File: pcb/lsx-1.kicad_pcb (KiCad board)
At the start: 2 copper layers, 25.4 x 27.9 mm, 7 parts, among them J1 RJ45, J2 USART-USB, J3 ISP

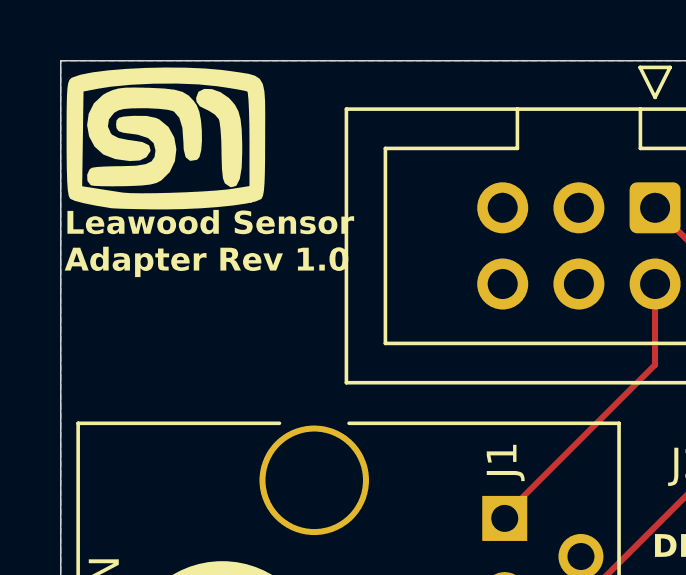
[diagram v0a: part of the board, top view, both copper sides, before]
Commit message: Corrects the GND on the ISP
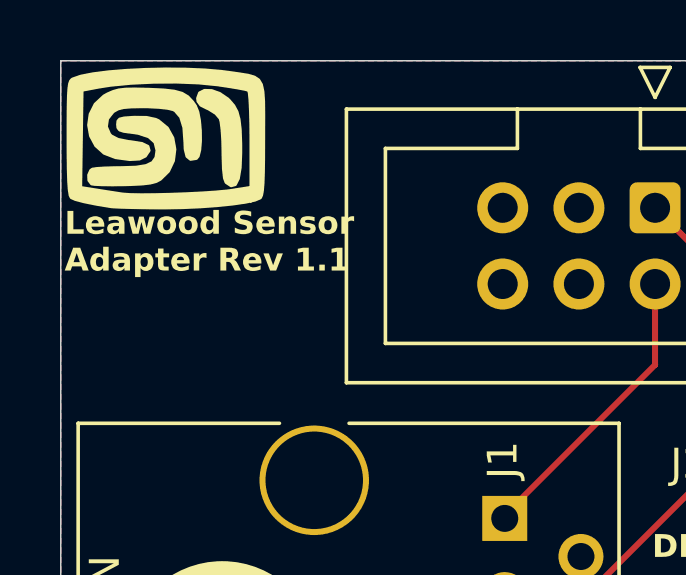
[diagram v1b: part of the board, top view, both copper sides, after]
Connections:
- J3 pad 6: unconnected-(J3-Pin_6-Pad6) -> GND
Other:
- board text added: "Leawood Sensor Adapter Rev 1.1"
- board text removed: "Leawood Sensor Adapter Rev 1.0"
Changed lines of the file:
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@@
 	(title_block
 		(title "Leawood Sensor Adapter LSX-1")
-		(date "2024-03-27")
-		(rev "1.0")
+		(date "2024-05-12")
+		(rev "1.1")
 	)
 	(layers
@@
 			(outputformat 1)
 			(mirror no)
-			(drillshape 1)
+			(drillshape 0)
 			(scaleselection 1)
-			(outputdirectory "")
+			(outputdirectory "lsx-Gerber/")
 		)
 	)
@@
 	(net 8 "unconnected-(J2-Pin_5-Pad5)")
 	(net 9 "unconnected-(J3-Pin_3-Pad3)")
-	(net 10 "unconnected-(J3-Pin_6-Pad6)")
-	(net 11 "unconnected-(J3-Pin_4-Pad4)")
-	(net 12 "unconnected-(J3-Pin_5-Pad5)")
+	(net 10 "unconnected-(J3-Pin_4-Pad4)")
+	(net 11 "unconnected-(J3-Pin_5-Pad5)")
 	(footprint "lsx-1-footprint:RJ45_8P8C"
 		(layer "F.Cu")
@@
 		)
 		(property "Value" "ISP"
-			(at 3.048 7.9756 270)
+			(at 3.048 7.9756 -90)
 			(layer "F.Fab")
 			(hide yes)
@@
 			(layers "*.Cu" "*.Mask")
 			(remove_unused_layers no)
-			(net 11 "unconnected-(J3-Pin_4-Pad4)")
+			(net 10 "unconnected-(J3-Pin_4-Pad4)")
 			(pinfunction "Pin_4")
 			(pintype "passive+no_connect")
@@
 			(layers "*.Cu" "*.Mask")
 			(remove_unused_layers no)
-			(net 12 "unconnected-(J3-Pin_5-Pad5)")
+			(net 11 "unconnected-(J3-Pin_5-Pad5)")
 			(pinfunction "Pin_5")
 			(pintype "passive+no_connect")
@@
 			(layers "*.Cu" "*.Mask")
 			(remove_unused_layers no)
-			(net 10 "unconnected-(J3-Pin_6-Pad6)")
+			(net 1 "GND")
 			(pinfunction "Pin_6")
-			(pintype "passive+no_connect")
+			(pintype "passive")
 		)
 		(model "${KICAD8_3DMODEL_DIR}/Connector_IDC.3dshapes/IDC-Header_2x03_P2.54mm_Vertical.wrl"
@@
 		)
 	)
-	(gr_text "Leawood Sensor\nAdapter Rev 1.0"
+	(gr_text "Leawood Sensor\nAdapter Rev 1.1"
 		(at 76.327 55.3466 0)
 		(layer "F.SilkS")
@@
 		)
 	)
+	(dimension
+		(type aligned)
+		(layer "User.1")
+		(pts
+			(xy 101.6 48.26) (xy 101.6 76.2)
+		)
+		(height -12.065)
+		(gr_text "27.9400 mm"
+			(at 112.776 62.23 90)
+			(layer "User.1")
+			(effects
+				(font
+					(size 0.762 0.762)
+					(thickness 0.127)
+				)
+			)
+		)
+		(format
+			(prefix "")
+			(suffix "")
+			(units 3)
+			(units_format 1)
+			(precision 4)
+		)
+		(style
+			(thickness 0.1)
+			(arrow_length 1.27)
+			(text_position_mode 0)
+			(extension_height 0.58642)
+			(extension_offset 0.5) keep_text_aligned)
+	)
+	(dimension
+		(type aligned)
+		(layer "User.1")
+		(pts
+			(xy 76.2 48.26) (xy 101.6 48.26)
+		)
+		(height -6.604)
+		(gr_text "25.4000 mm"
+			(at 88.9 40.767 0)
+			(layer "User.1")
+			(effects
+				(font
+					(size 0.762 0.762)
+					(thickness 0.127)
+				)
+			)
+		)
+		(format
+			(prefix "")
+			(suffix "")
+			(units 3)
+			(units_format 1)
+			(precision 4)
+		)
+		(style
+			(thickness 0.1)
+			(arrow_length 1.27)
+			(text_position_mode 0)
+			(extension_height 0.58642)
+			(extension_offset 0.5) keep_text_aligned)
+	)
 	(segment

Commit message: Update
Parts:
- added H1: MountingHole, MountingHole:MountingHole_2.7mm_M2.5, F.Cu at (53.0, 53.0)
- added H2: MountingHole, MountingHole:MountingHole_2.7mm_M2.5, F.Cu at (53.0, 92.0)
- added H3: MountingHole, MountingHole:MountingHole_2.7mm_M2.5, F.Cu at (77.0, 92.0)
- added H4: MountingHole, MountingHole:MountingHole_2.7mm_M2.5, F.Cu at (76.8, 53.0)
- J2: footprint Connector_PinSocket_2.54mm:PinSocket_1x06_P2.54mm_Vertical -> Connector_PinHeader_2.54mm:PinHeader_1x06_P2.54mm_Horizontal
- J3: footprint Connector_IDC:IDC-Header_2x03_P2.54mm_Vertical -> Connector_PinHeader_2.54mm:PinHeader_2x03_P2.54mm_Horizontal
- Lg2: moved to F.Cu
- moved Lg1 44.4 mm to (58.7, 89.9), turned to 90 degrees
- moved Lg2 32.6 mm to (68.6, 86.9), turned to 90 degrees
- moved J2 27.2 mm to (75.8, 74.5)
- moved J1 27.0 mm to (66.9, 76.7)
- moved Lg3 25.3 mm to (56.6, 72.4)
- moved Lg4 25.3 mm to (56.6, 72.4)
- moved J3 23.2 mm to (73.3, 57.9), turned to 0 degrees
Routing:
- net +3.3V: track 9.89 -> 18.8 mm
- net /UPDI: track 18.0 -> 21.9 mm
- net /DOUT: track 10.6 -> 13.8 mm
- net /DIN: track 10.6 -> 13.3 mm
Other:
- board size 25.4 x 27.9 mm -> 30 x 45 mm
- board text removed: "UPDI 3V3"
